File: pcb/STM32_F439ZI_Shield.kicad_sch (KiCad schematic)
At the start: 19 parts, among them K1 G6S-2, K2 G6S-2, U1 LM2904, U13 R-78E3.3-0.5, U14 R-78E5.0-0.5, U2 MAX3485

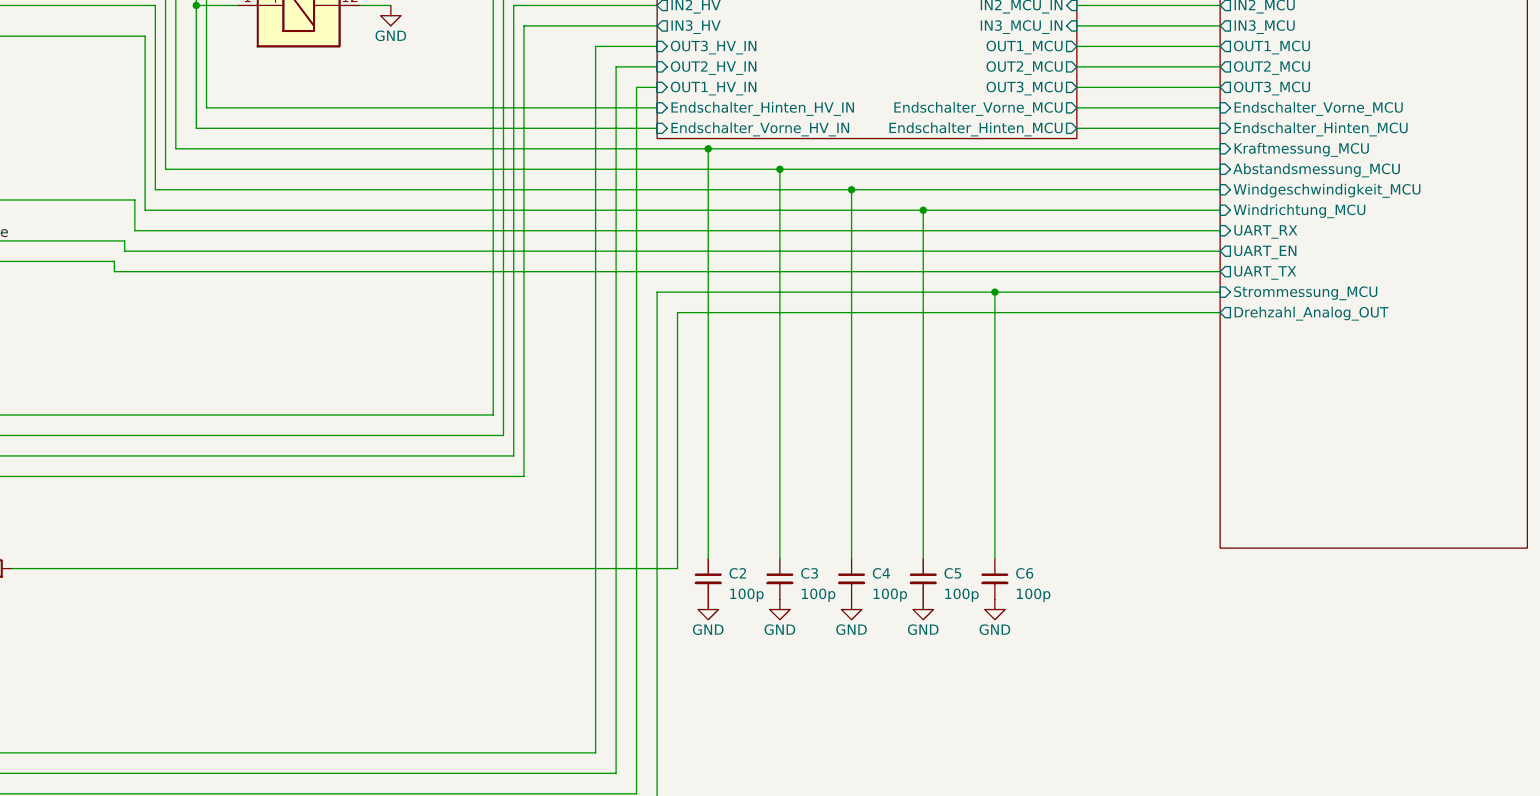
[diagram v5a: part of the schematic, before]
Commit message: added buttons & LEDs
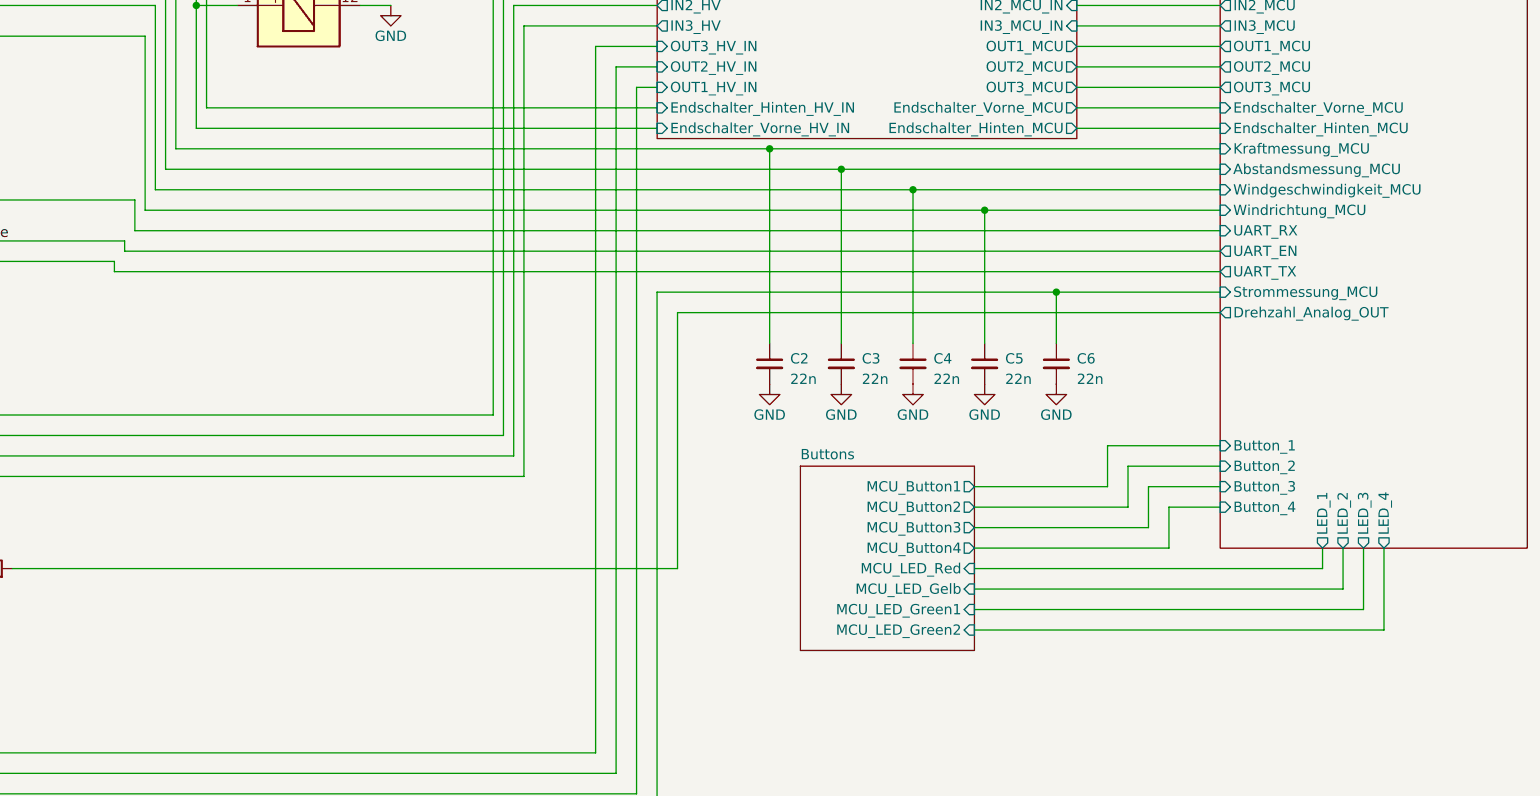
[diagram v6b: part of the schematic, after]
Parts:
- C2, C3, C4, C5, C6: value 100p -> 22n
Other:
- added sheet Buttons (Buttons.kicad_sch)
- sheet STM32F439ZI ports: added Button_1, Button_2, Button_3, Button_4, LED_1, LED_2, LED_3, LED_4; removed none
- moved on the sheet: C2, C3, C4, C5, C6

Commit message: Updated footprints
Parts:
- C1, C2, C3, C4, C5, C6: footprint Capacitor_SMD:C_0603_1608Metric -> Capacitor_SMD:C_1206_3216Metric
- F1: footprint (none) -> Fuse:Fuse_BelFuse_0ZRE0005FF_L8.3mm_W3.8mm
- R10: footprint Resistor_SMD:R_0603_1608Metric -> Resistor_SMD:R_1206_3216Metric
- R6, R7, R8, R9: footprint Resistor_SMD:R_0201_0603Metric -> Resistor_SMD:R_1206_3216Metric
- Spannungsversorgung_1: footprint (none) -> Connector_Phoenix_MSTB:PhoenixContact_MSTBA_2,5_2-G-5,08_1x02_P5.08mm_Horizontal
- U1: footprint (none) -> LM2904:SO08
- U2: footprint (none) -> MAX3485CSA_T:SOIC127P600X175-8N
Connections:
- net +3.3V: now also R7.1, U2.8 (VCC)
- net +5V: no longer R7.1, U2.8 (VCC)

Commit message: Save pcb cut out
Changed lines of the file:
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@@
   (junction (at 190.5 101.6) (diameter 0) (color 0 0 0 0)
   )
+  (junction (at 217.17 132.08) (diameter 0) (color 0 0 0 0)
+  )
   (junction (at 199.39 104.14) (diameter 0) (color 0 0 0 0)
   )
@@
   (junction (at 74.93 95.25) (diameter 0) (color 0 0 0 0)
   )
+  (junction (at 208.28 132.08) (diameter 0) (color 0 0 0 0)
+  )
   (junction (at 46.99 19.05) (diameter 0) (color 0 0 0 0)
   )
@@
   (junction (at 60.96 125.73) (diameter 0) (color 0 0 0 0)
   )
+  (junction (at 199.39 132.08) (diameter 0) (color 0 0 0 0)
+  )
   (junction (at 59.69 156.21) (diameter 0) (color 0 0 0 0)
   )
@@
     (stroke (width 0) (type default))
   )
+  (wire (pts (xy 226.06 130.81) (xy 226.06 132.08))
+    (stroke (width 0) (type default))
+  )
   (wire (pts (xy 45.72 142.24) (xy 160.02 142.24))
     (stroke (width 0) (type default))
@@
     (stroke (width 0) (type default))
   )
+  (wire (pts (xy 217.17 130.81) (xy 217.17 132.08))
+    (stroke (width 0) (type default))
+  )
   (wire (pts (xy 60.96 125.73) (xy 60.96 123.19))
     (stroke (width 0) (type default))
@@
     (stroke (width 0) (type default))
   )
+  (wire (pts (xy 190.5 132.08) (xy 199.39 132.08))
+    (stroke (width 0) (type default))
+  )
   (wire (pts (xy 121.92 12.7) (xy 237.49 12.7))
     (stroke (width 0) (type default))
@@
     (stroke (width 0) (type default))
   )
+  (wire (pts (xy 199.39 130.81) (xy 199.39 132.08))
+    (stroke (width 0) (type default))
+  )
   (wire (pts (xy 148.59 71.12) (xy 232.41 71.12))
     (stroke (width 0) (type default))
@@
     (stroke (width 0) (type default))
   )
+  (wire (pts (xy 190.5 130.81) (xy 190.5 132.08))
+    (stroke (width 0) (type default))
+  )
   (wire (pts (xy 171.45 179.07) (xy 171.45 91.44))
     (stroke (width 0) (type default))
@@
     (stroke (width 0) (type default))
   )
+  (wire (pts (xy 199.39 132.08) (xy 208.28 132.08))
+    (stroke (width 0) (type default))
+  )
+  (wire (pts (xy 208.28 130.81) (xy 208.28 132.08))
+    (stroke (width 0) (type default))
+  )
   (wire (pts (xy 237.49 148.59) (xy 237.49 143.51))
     (stroke (width 0) (type default))
@@
     (stroke (width 0) (type default))
   )
+  (wire (pts (xy 208.28 132.08) (xy 217.17 132.08))
+    (stroke (width 0) (type default))
+  )
   (wire (pts (xy 85.09 110.49) (xy 88.9 110.49))
+    (stroke (width 0) (type default))
+  )
+  (wire (pts (xy 217.17 132.08) (xy 226.06 132.08))
     (stroke (width 0) (type default))
   )
@@
     )
   )
-  (symbol (lib_id "power:GND") (at 199.39 130.81 0) (unit 1)
-    (in_bom yes) (on_board yes) (dnp no)
-    (property "Reference" "#PWR067" (at 199.39 137.16 0)
-      (effects (font (size 1.27 1.27)) hide)
-    )
-    (property "Value" "GND" (at 199.39 134.62 0)
-      (effects (font (size 1.27 1.27)))
-    )
-    (property "Footprint" "" (at 199.39 130.81 0)
-      (effects (font (size 1.27 1.27)) hide)
-    )
-    (property "Datasheet" "" (at 199.39 130.81 0)
-      (effects (font (size 1.27 1.27)) hide)
-    )
-    (pin "1")
-    (instances
-      (project "STM32_F439ZI_Shield"
-        (path "/19bff231-ff37-4a40-bd06-2039e9f55c77"
-          (reference "#PWR067") (unit 1)
-        )
-      )
-    )
-  )
   (symbol (lib_id "power:GND") (at 59.69 170.18 0) (unit 1)
     (in_bom yes) (on_board yes) (dnp no)
@@
         (path "/19bff231-ff37-4a40-bd06-2039e9f55c77"
           (reference "#PWR029") (unit 1)
-        )
-      )
-    )
-  )
-  (symbol (lib_id "power:GND") (at 226.06 130.81 0) (unit 1)
-    (in_bom yes) (on_board yes) (dnp no)
-    (property "Reference" "#PWR070" (at 226.06 137.16 0)
-      (effects (font (size 1.27 1.27)) hide)
-    )
-    (property "Value" "GND" (at 226.06 134.62 0)
-      (effects (font (size 1.27 1.27)))
-    )
-    (property "Footprint" "" (at 226.06 130.81 0)
-      (effects (font (size 1.27 1.27)) hide)
-    )
-    (property "Datasheet" "" (at 226.06 130.81 0)
-      (effects (font (size 1.27 1.27)) hide)
-    )
-    (pin "1")
-    (instances
-      (project "STM32_F439ZI_Shield"
-        (path "/19bff231-ff37-4a40-bd06-2039e9f55c77"
-          (reference "#PWR070") (unit 1)
         )
       )
@@
         (path "/19bff231-ff37-4a40-bd06-2039e9f55c77"
           (reference "#PWR019") (unit 1)
-        )
-      )
-    )
-  )
-  (symbol (lib_id "power:GND") (at 208.28 130.81 0) (unit 1)
-    (in_bom yes) (on_board yes) (dnp no)
-    (property "Reference" "#PWR068" (at 208.28 137.16 0)
-      (effects (font (size 1.27 1.27)) hide)
-    )
-    (property "Value" "GND" (at 208.28 134.62 0)
-      (effects (font (size 1.27 1.27)))
-    )
-    (property "Footprint" "" (at 208.28 130.81 0)
-      (effects (font (size 1.27 1.27)) hide)
-    )
-    (property "Datasheet" "" (at 208.28 130.81 0)
-      (effects (font (size 1.27 1.27)) hide)
-    )
-    (pin "1")
-    (instances
-      (project "STM32_F439ZI_Shield"
-        (path "/19bff231-ff37-4a40-bd06-2039e9f55c77"
-          (reference "#PWR068") (unit 1)
         )
       )
@@
     )
   )
+  (symbol (lib_id "power:GND") (at 208.28 132.08 0) (unit 1)
+    (in_bom yes) (on_board yes) (dnp no)
+    (property "Reference" "#PWR066" (at 208.28 138.43 0)
+      (effects (font (size 1.27 1.27)) hide)
+    )
+    (property "Value" "GND" (at 208.28 135.89 0)
+      (effects (font (size 1.27 1.27)))
+    )
+    (property "Footprint" "" (at 208.28 132.08 0)
+      (effects (font (size 1.27 1.27)) hide)
+    )
+    (property "Datasheet" "" (at 208.28 132.08 0)
+      (effects (font (size 1.27 1.27)) hide)
+    )
+    (pin "1")
+    (instances
+      (project "STM32_F439ZI_Shield"
+        (path "/19bff231-ff37-4a40-bd06-2039e9f55c77"
+          (reference "#PWR066") (unit 1)
+        )
+      )
+    )
+  )
   (symbol (lib_id "power:GND") (at 143.51 46.99 0) (unit 1)
     (in_bom yes) (on_board yes) (dnp no)
@@
     )
   )
-  (symbol (lib_id "power:GND") (at 217.17 130.81 0) (unit 1)
-    (in_bom yes) (on_board yes) (dnp no)
-    (property "Reference" "#PWR069" (at 217.17 137.16 0)
-      (effects (font (size 1.27 1.27)) hide)
-    )
-    (property "Value" "GND" (at 217.17 134.62 0)
-      (effects (font (size 1.27 1.27)))
-    )
-    (property "Footprint" "" (at 217.17 130.81 0)
-      (effects (font (size 1.27 1.27)) hide)
-    )
-    (property "Datasheet" "" (at 217.17 130.81 0)
-      (effects (font (size 1.27 1.27)) hide)
-    )
-    (pin "1")
-    (instances
-      (project "STM32_F439ZI_Shield"
-        (path "/19bff231-ff37-4a40-bd06-2039e9f55c77"
-          (reference "#PWR069") (unit 1)
-        )
-      )
-    )
-  )
   (symbol (lib_id "Regulator_Switching:R-78E3.3-0.5") (at 59.69 19.05 0) (unit 1)
     (in_bom yes) (on_board yes) (dnp no)
@@
         )
       )
-    )
-  )
-  (symbol (lib_id "power:GND") (at 190.5 130.81 0) (unit 1)
-    (in_bom yes) (on_board yes) (dnp no)
-    (property "Reference" "#PWR066" (at 190.5 137.16 0)
-      (effects (font (size 1.27 1.27)) hide)
-    )
-    (property "Value" "GND" (at 190.5 134.62 0)
-      (effects (font (size 1.27 1.27)))
-    )
-    (property "Footprint" "" (at 190.5 130.81 0)
-      (effects (font (size 1.27 1.27)) hide)
-    )
-    (property "Datasheet" "" (at 190.5 130.81 0)
-      (effects (font (size 1.27 1.27)) hide)
-    )
-    (pin "1")
-    (instances
-      (project "STM32_F439ZI_Shield"
-        (path "/19bff231-ff37-4a40-bd06-2039e9f55c77"
-          (reference "#PWR066") (unit 1)
-        )
-      )
